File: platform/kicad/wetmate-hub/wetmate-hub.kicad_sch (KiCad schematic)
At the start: 2 parts, among them J1 Screw_Terminal_01x04, J2 Screw_Terminal_01x02

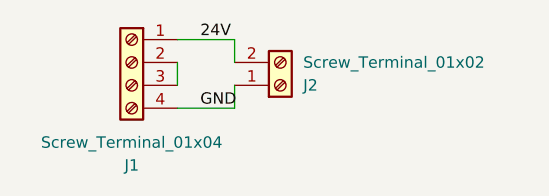
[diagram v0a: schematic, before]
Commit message: Wetmate Hub: Finalise layout for production
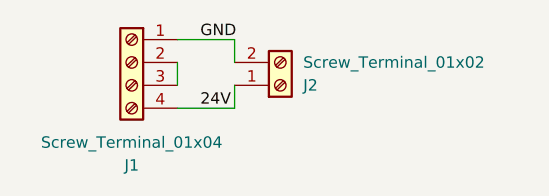
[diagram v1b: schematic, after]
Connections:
- net 24V: now also J1.4 (Pin_4), J2.1 (Pin_1); no longer J1.1 (Pin_1), J2.2 (Pin_2)
- net GND: now also J1.1 (Pin_1), J2.2 (Pin_2); no longer J1.4 (Pin_4), J2.1 (Pin_1)
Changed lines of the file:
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@@
 		)
 	)
-	(label "24V"
+	(label "GND"
 		(at 129.54 76.2 0)
 		(fields_autoplaced yes)
@@
 		)
 	)
-	(label "GND"
+	(label "24V"
 		(at 129.54 83.82 0)
 		(fields_autoplaced yes)
